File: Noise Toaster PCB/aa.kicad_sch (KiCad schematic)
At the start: 14 parts, among them U4 LM386, X12 Conn_01x01_Pin

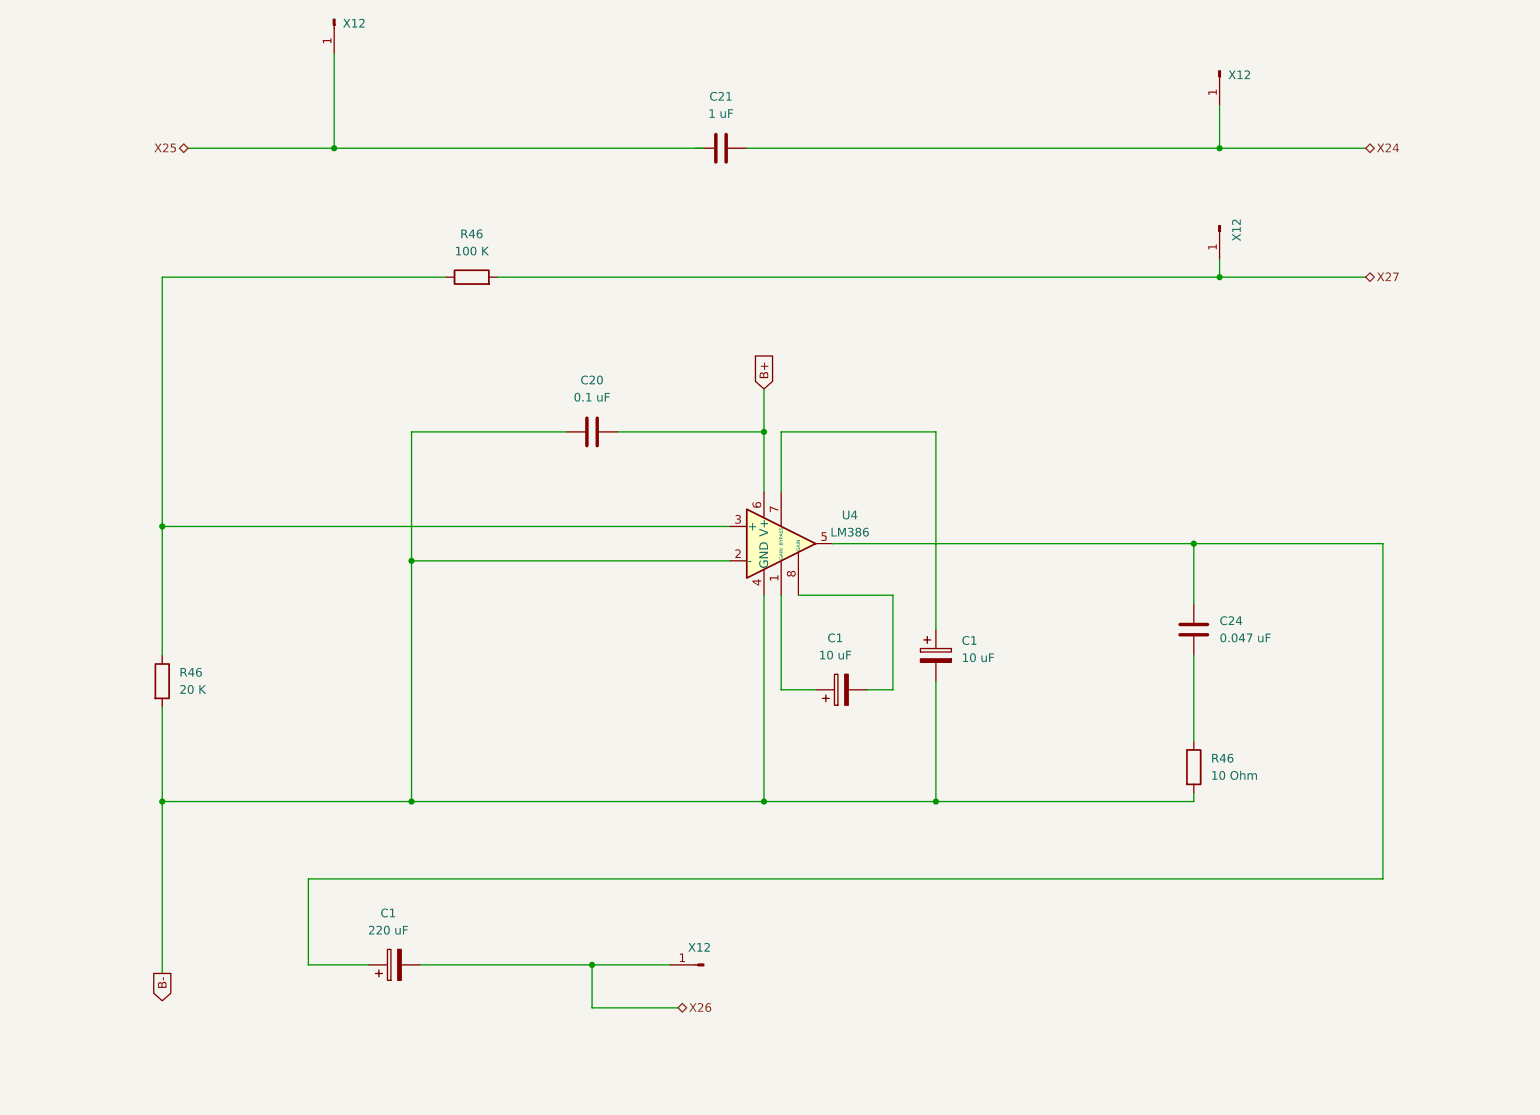
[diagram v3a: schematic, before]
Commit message: wireing and components have been checked
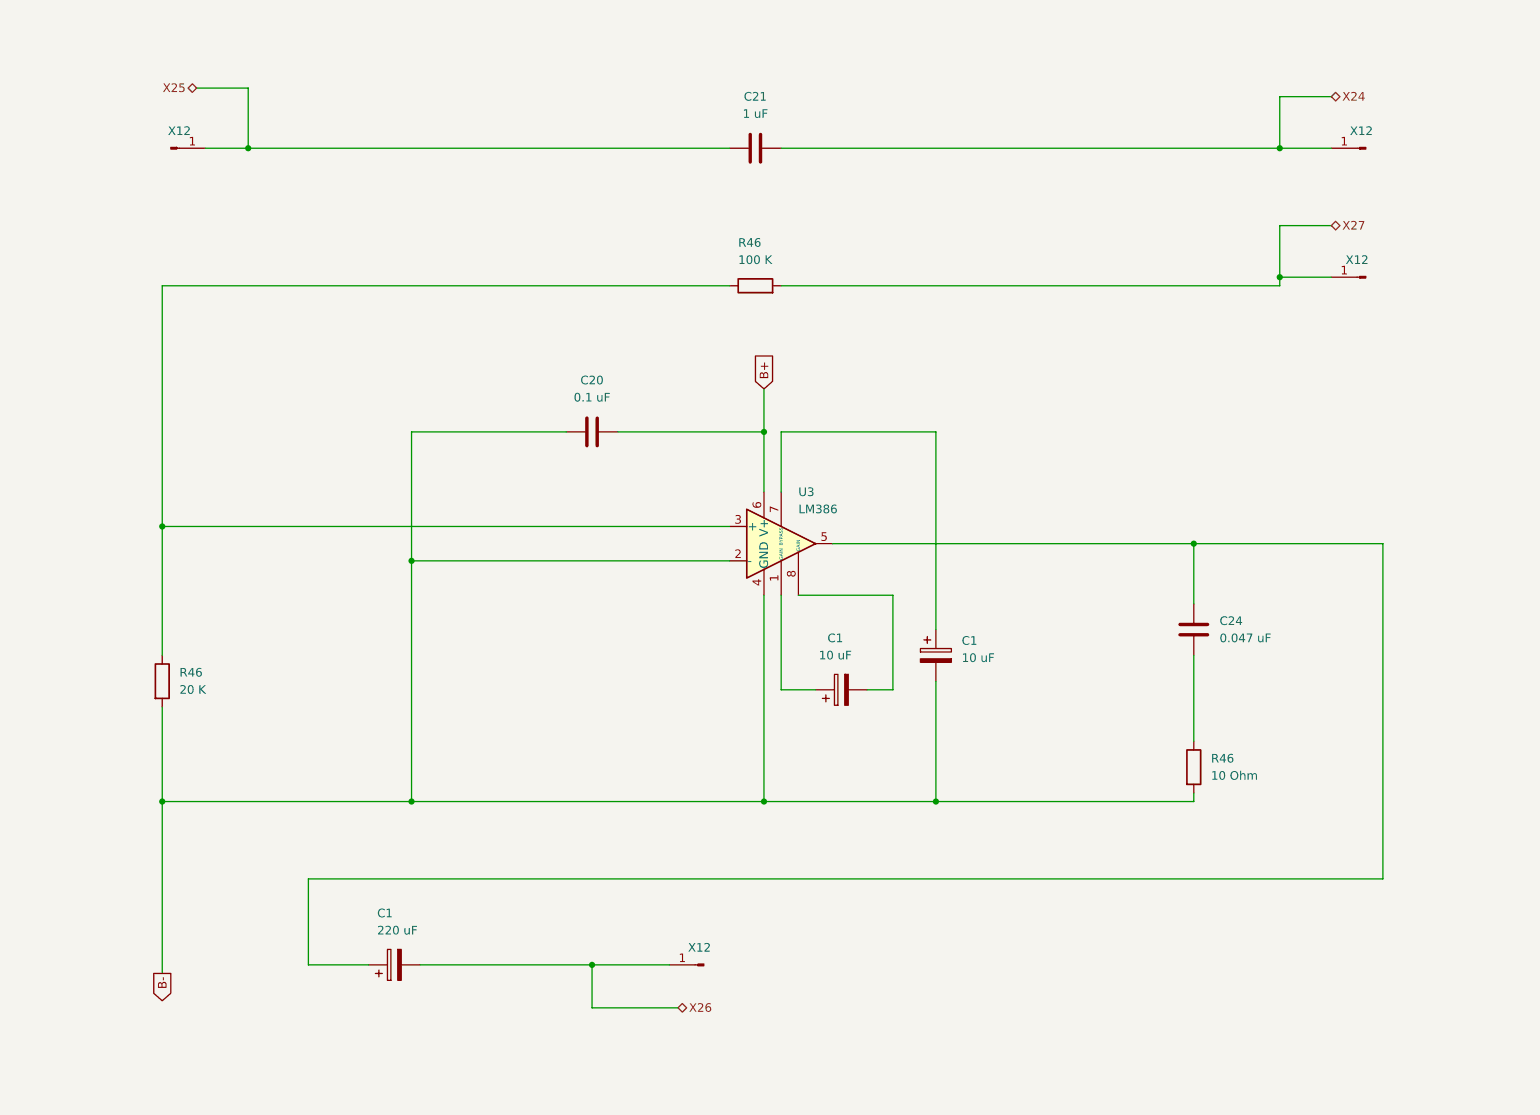
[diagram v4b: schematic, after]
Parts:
- renumbered U4 to U3
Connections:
- net X25: now also C21.1
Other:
- moved on the sheet: C21, R46, X12

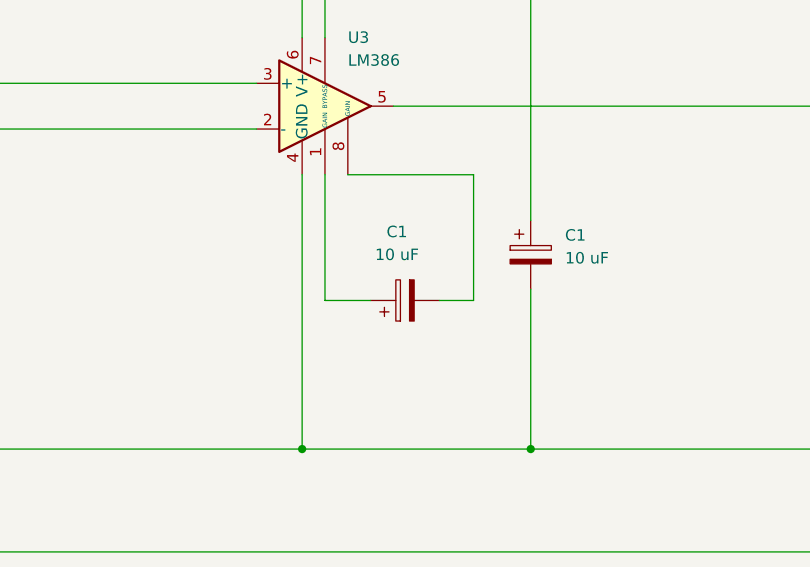
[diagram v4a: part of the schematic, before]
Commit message: applied footprints
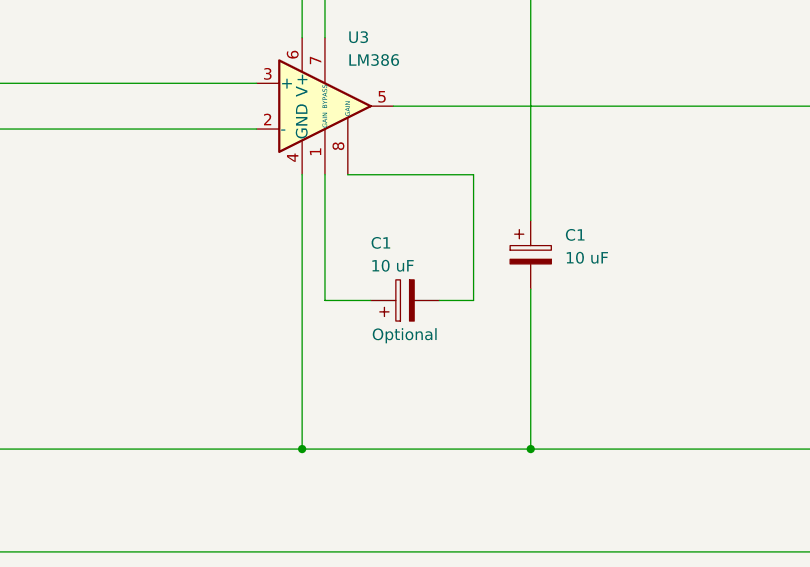
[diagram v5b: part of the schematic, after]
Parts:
- C1: footprint (none) -> Capacitor_THT:CP_Radial_D4.0mm_P1.50mm
- C1: footprint (none) -> Capacitor_THT:CP_Radial_D10.0mm_P5.00mm
- C1: footprint (none) -> Capacitor_THT:CP_Radial_D4.0mm_P1.50mm; Feld4 (none) -> Optional
- C20, C24: footprint (none) -> Capacitor_THT:C_Disc_D5.1mm_W3.2mm_P5.00mm
- C21: footprint (none) -> Capacitor_THT:CP_Axial_L20.0mm_D10.0mm_P26.00mm_Horizontal
- R46: footprint (none) -> Resistor_THT:R_Axial_DIN0207_L6.3mm_D2.5mm_P10.16mm_Horizontal
- U3: footprint (none) -> Package_DIP:DIP-8_W7.62mm_Socket
- X12: footprint (none) -> Connector_PinHeader_1.00mm:PinHeader_1x01_P1.00mm_Vertical
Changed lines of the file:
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@@
       (effects (font (size 1.27 1.27)) (justify left) hide)
     )
-    (property "Footprint" "" (at 130.81 165.1 0)
+    (property "Footprint" "Connector_PinHeader_1.00mm:PinHeader_1x01_P1.00mm_Vertical" (at 130.81 165.1 0)
       (effects (font (size 1.27 1.27)) hide)
     )
@@
       (effects (font (size 1.27 1.27)) (justify left))
     )
-    (property "Footprint" "" (at 144.78 100.33 0)
+    (property "Footprint" "Package_DIP:DIP-8_W7.62mm_Socket" (at 144.78 100.33 0)
       (effects (font (size 1.27 1.27)) hide)
     )
@@
       (effects (font (size 1.27 1.27)) (justify left))
     )
-    (property "Footprint" "" (at 201.422 135.89 90)
+    (property "Footprint" "Resistor_THT:R_Axial_DIN0207_L6.3mm_D2.5mm_P10.16mm_Horizontal" (at 201.422 135.89 90)
       (effects (font (size 1.27 1.27)) hide)
     )
@@
       (effects (font (size 1.27 1.27)) (justify left) hide)
     )
-    (property "Footprint" "" (at 228.6 63.5 0)
+    (property "Footprint" "Connector_PinHeader_1.00mm:PinHeader_1x01_P1.00mm_Vertical" (at 228.6 63.5 0)
       (effects (font (size 1.27 1.27)) hide)
     )
@@
       (effects (font (size 1.27 1.27)) (justify left))
     )
-    (property "Footprint" "" (at 204.1652 119.38 0)
+    (property "Footprint" "Capacitor_THT:C_Disc_D5.1mm_W3.2mm_P5.00mm" (at 204.1652 119.38 0)
       (effects (font (size 1.27 1.27)) hide)
     )
@@
       (effects (font (size 1.27 1.27)))
     )
-    (property "Footprint" "" (at 118.11 85.3948 0)
+    (property "Footprint" "Capacitor_THT:C_Disc_D5.1mm_W3.2mm_P5.00mm" (at 118.11 85.3948 0)
       (effects (font (size 1.27 1.27)) hide)
     )
@@
       (effects (font (size 1.27 1.27)) (justify left) hide)
     )
-    (property "Footprint" "" (at 52.07 44.45 0)
+    (property "Footprint" "Connector_PinHeader_1.00mm:PinHeader_1x01_P1.00mm_Vertical" (at 52.07 44.45 0)
       (effects (font (size 1.27 1.27)) hide)
     )
@@
       (effects (font (size 1.27 1.27)) (justify left))
     )
-    (property "Footprint" "" (at 166.0652 123.19 0)
+    (property "Footprint" "Capacitor_THT:CP_Radial_D4.0mm_P1.50mm" (at 166.0652 123.19 0)
       (effects (font (size 1.27 1.27)) hide)
     )
@@
       (effects (font (size 1.27 1.27)) (justify left) hide)
     )
-    (property "Footprint" "" (at 228.6 44.45 0)
+    (property "Footprint" "Connector_PinHeader_1.00mm:PinHeader_1x01_P1.00mm_Vertical" (at 228.6 44.45 0)
       (effects (font (size 1.27 1.27)) hide)
     )
@@
       (effects (font (size 1.27 1.27)) (justify right))
     )
-    (property "Footprint" "" (at 88.9 164.1348 0)
+    (property "Footprint" "Capacitor_THT:CP_Radial_D10.0mm_P5.00mm" (at 88.9 164.1348 0)
       (effects (font (size 1.27 1.27)) hide)
     )
@@
       (effects (font (size 1.27 1.27)) (justify left))
     )
-    (property "Footprint" "" (at 49.022 123.19 90)
+    (property "Footprint" "Resistor_THT:R_Axial_DIN0207_L6.3mm_D2.5mm_P10.16mm_Horizontal" (at 49.022 123.19 90)
       (effects (font (size 1.27 1.27)) hide)
     )
@@
   )
   (symbol (lib_id "Device:C_Polarized") (at 151.13 124.46 90) (unit 1)
-    (in_bom yes) (on_board yes) (dnp no) (fields_autoplaced)
-    (property "Reference" "C1" (at 150.241 116.84 90)
-      (effects (font (size 1.27 1.27)))
-    )
-    (property "Value" "10 uF" (at 150.241 119.38 90)
-      (effects (font (size 1.27 1.27)))
-    )
-    (property "Footprint" "" (at 154.94 123.4948 0)
+    (in_bom yes) (on_board yes) (dnp no)
+    (property "Reference" "C1" (at 147.32 118.11 90)
+      (effects (font (size 1.27 1.27)) (justify right))
+    )
+    (property "Value" "10 uF" (at 147.32 120.65 90)
+      (effects (font (size 1.27 1.27)) (justify right))
+    )
+    (property "Footprint" "Capacitor_THT:CP_Radial_D4.0mm_P1.50mm" (at 154.94 123.4948 0)
       (effects (font (size 1.27 1.27)) hide)
     )
     (property "Datasheet" "~" (at 151.13 124.46 0)
       (effects (font (size 1.27 1.27)) hide)
+    )
+    (property "Feld4" "Optional" (at 151.13 128.27 90)
+      (effects (font (size 1.27 1.27)))
     )
     (pin "1")
@@
         )
         (path "/7be3f398-d902-4566-9ee4-0bff072cd47e/8b7babf3-8af2-4de0-abdc-510e7f40fd33"
-          (reference "Optional") (unit 1)
+          (reference "C27") (unit 1)
         )
       )
@@
       (effects (font (size 1.27 1.27)) (justify right))
     )
-    (property "Footprint" "" (at 138.43 66.548 90)
+    (property "Footprint" "Resistor_THT:R_Axial_DIN0207_L6.3mm_D2.5mm_P10.16mm_Horizontal" (at 138.43 66.548 90)
       (effects (font (size 1.27 1.27)) hide)
     )
@@
       (effects (font (size 1.27 1.27)))
     )
-    (property "Footprint" "" (at 142.24 43.4848 0)
-      (effects (font (size 1.27 1.27)) hide)
-    )
+    (property "Footprint" "Capacitor_THT:CP_Axial_L20.0mm_D10.0mm_P26.00mm_Horizontal" (at 142.24 43.4848 0)
+      (effects (font (size 1.27 1.27)) hide)
+    )

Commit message: placed pards of the pcb properly
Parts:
- C21: footprint Capacitor_THT:CP_Axial_L20.0mm_D10.0mm_P26.00mm_Horizontal -> Capacitor_THT:CP_Radial_D5.0mm_P2.00mm
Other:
- company: http://musicfromouterspace.com/analogsynth_new/NOISETOASTER/NOISETOASTER.php -> Music From Outer Space LLC
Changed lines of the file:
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@@
     (title "Audio Amplifier")
     (rev "0.5")
-    (company "http://musicfromouterspace.com/analogsynth_new/NOISETOASTER/NOISETOASTER.php")
+    (company "Music From Outer Space LLC")
     (comment 1 "Licence: CC-BY-NC-SA")
     (comment 2 "Original Design by Ray Wilson")
-    (comment 3 "Music From Outer Space LLC")
+    (comment 3 "http://musicfromouterspace.com/analogsynth_new/NOISETOASTER/NOISETOASTER.php")
   )
   (junction (at 139.7 140.97) (diameter 0) (color 0 0 0 0)
@@
       (effects (font (size 1.27 1.27)))
     )
-    (property "Footprint" "Capacitor_THT:CP_Axial_L20.0mm_D10.0mm_P26.00mm_Horizontal" (at 142.24 43.4848 0)
-      (effects (font (size 1.27 1.27)) hide)
-    )
+    (property "Footprint" "Capacitor_THT:CP_Radial_D5.0mm_P2.00mm" (at 142.24 43.4848 0)
+      (effects (font (size 1.27 1.27)) hide)
+    )
